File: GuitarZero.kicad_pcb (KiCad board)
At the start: 6 copper layers, 144 parts, among them J1 USB_A, J2 USB_B_Micro, J3 AudioJack3_SwitchT, J4 MCU_Debug, J6 Micro_SD_Card_Det_Hirose_DM3AT, SW1 SW_Push, SW2 SW_Push, SW3 SW_Push, SW4 SW_Push, SW5 SW_Push, SW6 SW_Push, U1 TPS54325, U10 FPGA_GPIO_Extra, U11 5x7 LED_matrix, U12 MCU_GPIO_Extra, U13 5x7 LED_matrix, U14 Power_Jumpers, U2 TSP54294, U3 XC7A100T-FTG256, U4 EFM32GG332, U5 S25FL127S, U6 Oscillator, U7 FPGA_JTAG_Debug, U8 PCM1754, U9 TPD_Current_Switch, Y1 Crystal_GND23

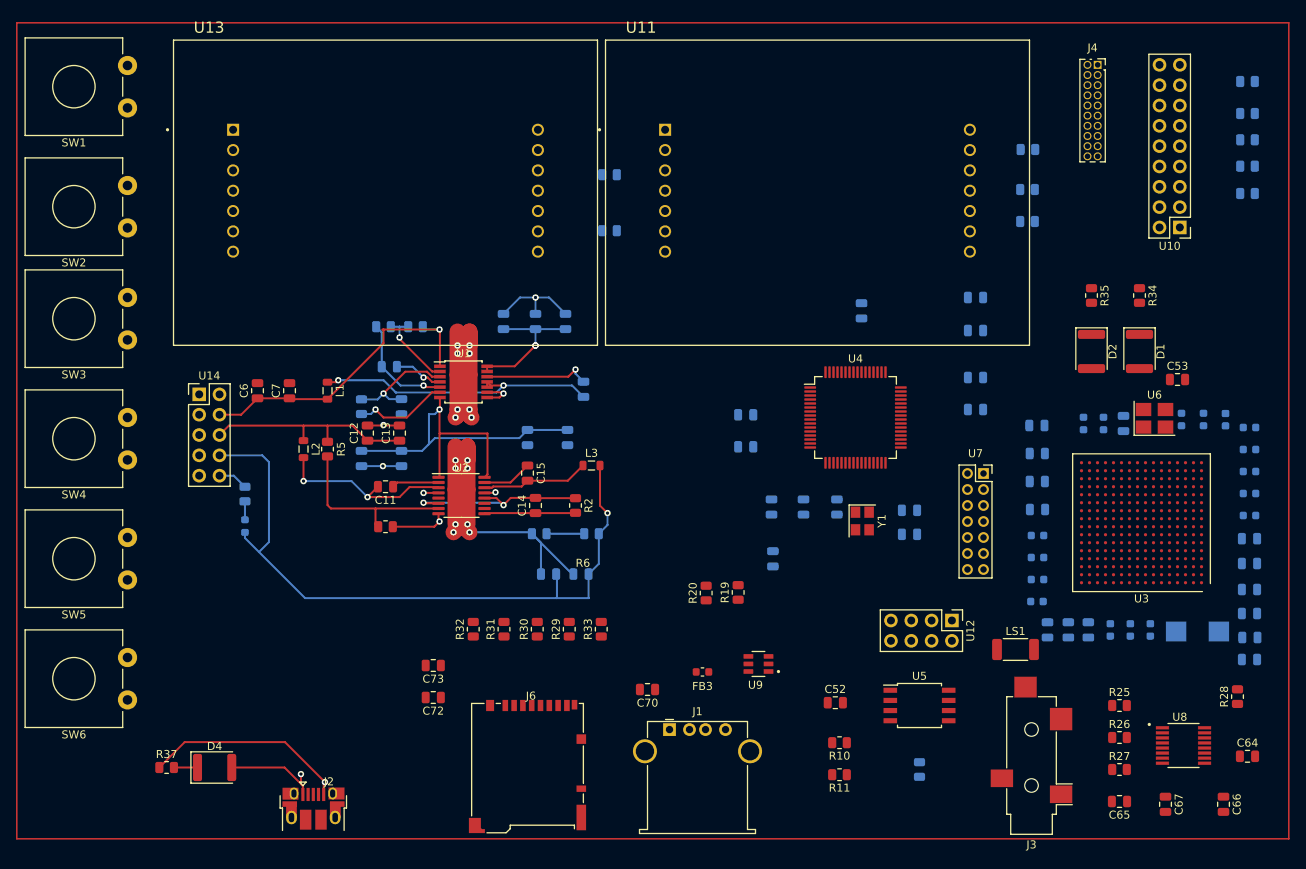
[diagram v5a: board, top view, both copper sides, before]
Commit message: Wired MCU in .pcb
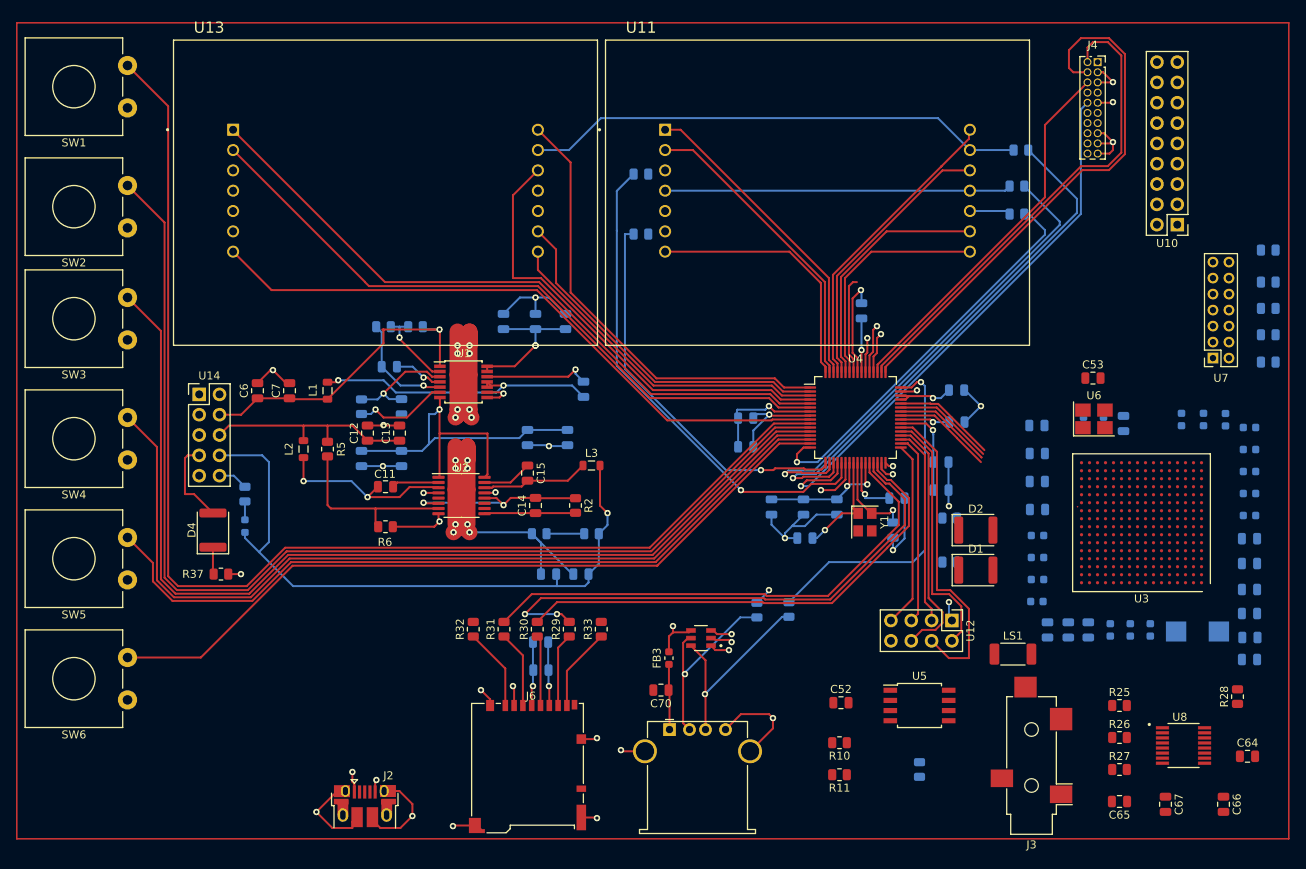
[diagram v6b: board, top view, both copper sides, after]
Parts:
- C72, C73, R19, R20, R34, R35: moved to B.Cu
- moved R34 40.9 mm to (173.8, 108.1), turned to 180 degrees
- moved D1 34.1 mm to (177.0, 109.1), turned to 0 degrees
- moved R35 33.0 mm to (173.8, 102.6), turned to 180 degrees
- moved U7 32.1 mm to (206.7, 82.6), turned to 180 degrees
- moved D4 29.7 mm to (81.7, 104.1), turned to 90 degrees
- moved D2 26.6 mm to (177.0, 104.1), turned to 0 degrees
- moved R37 25.1 mm to (82.7, 109.6), turned to 180 degrees
- moved R13 21.2 mm to (213.6, 69.1)
- moved R14 21.2 mm to (213.6, 73.1)
- moved R16 21.2 mm to (213.6, 79.7)
- moved R17 21.2 mm to (213.6, 83.1)
- moved R15 21.2 mm to (213.6, 76.4)
- moved C55 21.0 mm to (172.7, 95.6)
- moved C54 20.4 mm to (172.7, 99.1)
- moved C59 17.3 mm to (167.2, 100.1), turned to 0 degrees
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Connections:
- D4 pad 2: +5V -> +3.3V
- R18 pad 1: Net-(U11-R5) -> Net-(U11-R2)
- R21 pad 1: Net-(U11-R4) -> Net-(U11-R1)
- R23 pad 1: Net-(U11-R2) -> Net-(U11-R5)
- R24 pad 1: Net-(U11-R1) -> Net-(U11-R4)
- U11 pad 12: Net-(U4-PE12) -> Net-(U4-PE11)
- U11 pad 5: Net-(U4-PE12) -> unconnected-(U11-C4-Pad5)
- U13 pad 12: Net-(U4-PC3) -> Net-(U4-PA3)
- U13 pad 4: Net-(R22-Pad1) -> unconnected-(U13-R3-Pad4)
- U13 pad 5: Net-(U4-PC3) -> unconnected-(U13-C4-Pad5)
- U4 pad 1: /MCU/Button 1 -> Net-(U13-C6)
- U4 pad 10: Net-(U13-C2) -> /MCU/Button 1
- U4 pad 11: Net-(U13-C3) -> /MCU/Button 2
- U4 pad 12: Net-(U4-PC3) -> /MCU/Button 3
- U4 pad 13: Net-(U13-C5) -> /MCU/Button 4
- U4 pad 14: Net-(U13-C6) -> /MCU/Button 5
- U4 pad 15: Net-(U13-C7) -> /MCU/Button 6
- U4 pad 2: /MCU/Button 2 -> Net-(U13-C7)
- U4 pad 3: /MCU/Button 3 -> Net-(U13-C5)
- U4 pad 37: Net-(U12-GPIO_4) -> Net-(U12-GPIO_2)
- U4 pad 38: Net-(U12-GPIO_2) -> Net-(U12-GPIO_4)
- U4 pad 4: /MCU/Button 4 -> Net-(U4-PA3)
- U4 pad 5: /MCU/Button 5 -> Net-(U13-C3)
- U4 pad 58: Net-(U11-C1) -> Net-(U11-C5)
- U4 pad 59: Net-(U11-C2) -> Net-(U11-C7)
- U4 pad 6: /MCU/Button 6 -> Net-(U13-C1)
- U4 pad 60: Net-(U11-C3) -> Net-(U4-PE11)
- U4 pad 61: Net-(U4-PE12) -> Net-(U11-C6)
- U4 pad 62: Net-(U11-C5) -> Net-(U11-C3)
- U4 pad 63: Net-(U11-C6) -> Net-(U11-C1)
- U4 pad 64: Net-(U11-C7) -> Net-(U11-C2)
- U4 pad 9: Net-(U13-C1) -> Net-(U13-C2)
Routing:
- net /MCU/Button 1: track 0.00 -> 155.1 mm
- net /MCU/Button 2: track 0.00 -> 140.7 mm
- net GND: track 143.0 -> 270.6 mm, vias 25 -> 49
- net /MCU/Button 3: track 0.00 -> 127.2 mm
- net /MCU/Button 4: track 0.00 -> 112.8 mm
- net /MCU/Button 5: track 0.00 -> 98.3 mm
- net /MCU/Button 6: track 0.00 -> 96.4 mm
- net Net-(U13-C3): track 0.00 -> 86.3 mm
- net Net-(U13-C1): track 0.00 -> 85.5 mm
- net Net-(U13-C2): track 0.00 -> 80.9 mm
- net Net-(J4-RESET): track 0.00 -> 69.9 mm, vias 0 -> 1
- net +3.3V: track 0.00 -> 68.0 mm, vias 0 -> 6
- net Net-(U4-PD1): track 0.00 -> 67.9 mm, vias 0 -> 2
- net Net-(J4-SWCLK): track 0.00 -> 67.3 mm
- net Net-(J6-DAT3/CD): track 0.00 -> 66.2 mm, vias 0 -> 2
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
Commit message: completed DAC
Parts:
- moved C66 8.37 mm to (199.7, 137.6)
- moved C67 3.01 mm to (203.7, 137.6)
- moved R27 1.22 mm to (194.2, 133.1)
- moved C65 0.70 mm to (195.7, 138.0)
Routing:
- net GND: track 270.6 -> 319.7 mm, vias 49 -> 53
- net /DAC/OUT_RIGHT: track 0.00 -> 25.6 mm
- net /DAC/OUT_LEFT: track 0.00 -> 19.9 mm
- net +5V: track 201.7 -> 210.3 mm
- net Net-(U8-VoutL): track 0.00 -> 7.02 mm
- net Net-(U8-LRCK): track 0.00 -> 6.47 mm
- net Net-(U8-BCK): track 0.00 -> 5.61 mm
- net Net-(U8-SCK): track 0.00 -> 5.35 mm
- net Net-(U8-VoutR): track 0.00 -> 4.77 mm
- net Net-(U8-DATA): track 0.00 -> 4.70 mm
- net Net-(U8-Vcom): track 0.00 -> 4.52 mm
- net Net-(J3-PadTN): track 0.00 -> 4.43 mm

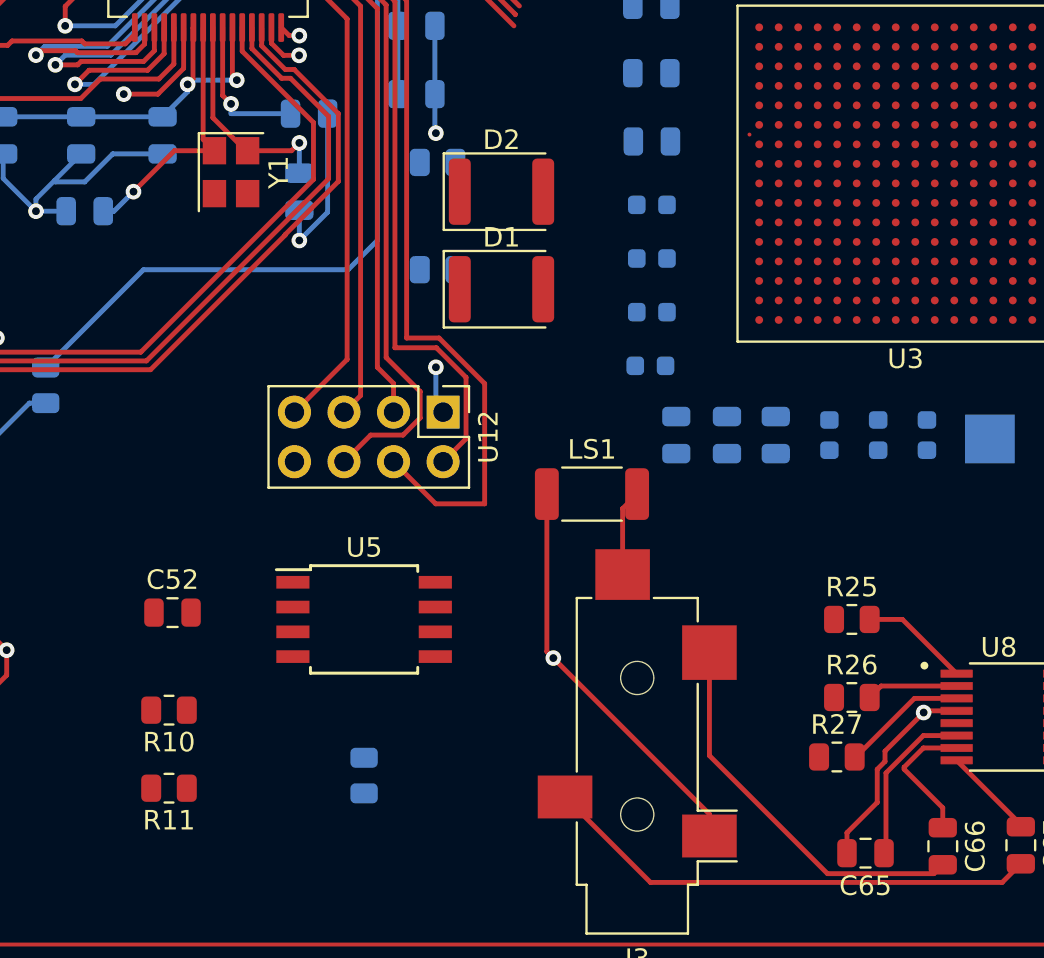
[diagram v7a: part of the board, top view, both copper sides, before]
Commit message: FPGA - SPI Flash Memory
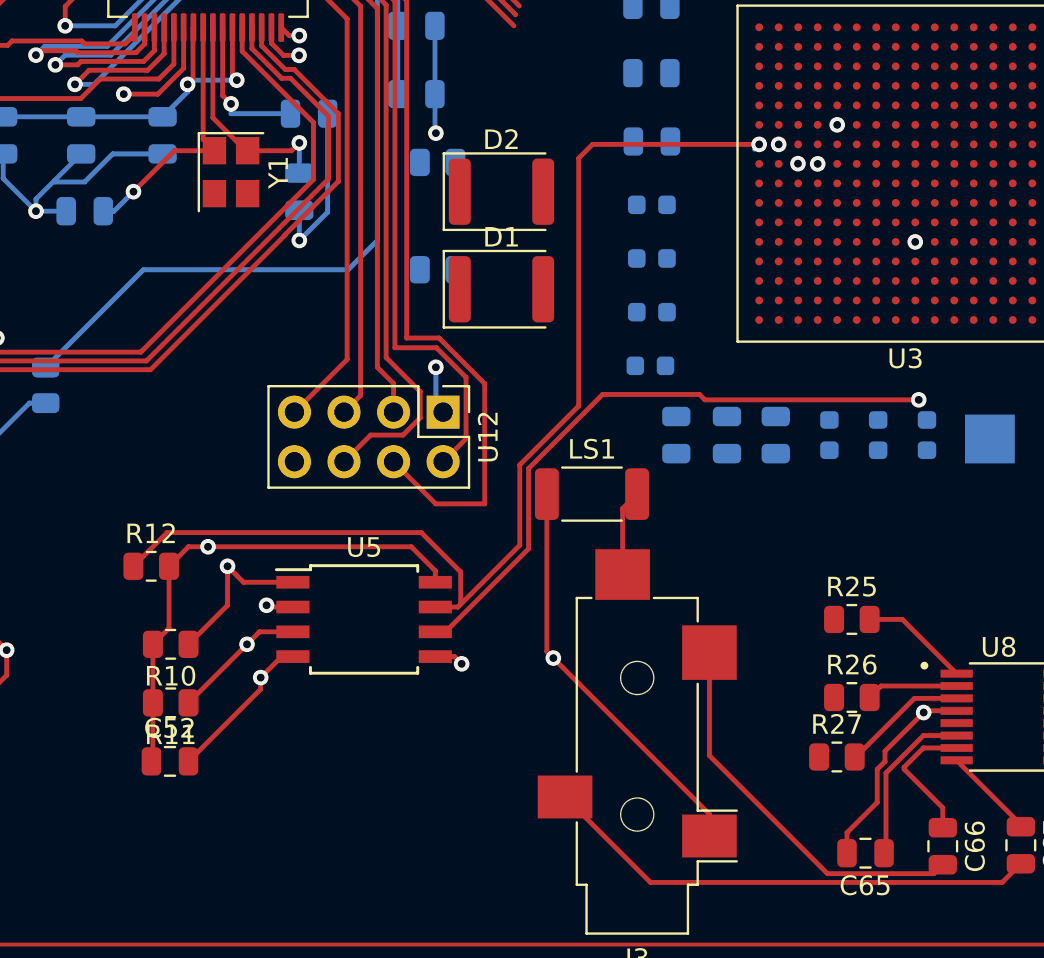
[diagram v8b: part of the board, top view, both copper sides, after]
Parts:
- R12: moved to F.Cu
- moved R12 15.3 mm to (159.1, 123.3), turned to 0 degrees
- moved C52 7.63 mm to (160.1, 133.3)
- moved R11 4.38 mm to (160.1, 130.3)
- moved R10 3.38 mm to (160.1, 127.3)
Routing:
- net Net-(U3A-IO_L6P_T0_FCS_B_14): track 0.00 -> 57.8 mm, vias 0 -> 2
- net Net-(U3A-IO_L2N_T0_D03_14): track 0.00 -> 56.6 mm, vias 0 -> 1
- net Net-(U3A-IO_L2P_T0_D02_14): track 0.00 -> 53.4 mm, vias 0 -> 2
- net Net-(U3A-IO_L1P_T0_D00_MOSI_14): track 0.00 -> 49.5 mm, vias 0 -> 2
- net Net-(U3A-IO_L1N_T0_D01_DIN_14): track 0.00 -> 45.8 mm, vias 0 -> 2
- net Net-(U3C-CCLK_0): track 0.00 -> 41.4 mm, vias 0 -> 2
- net +3.3V: track 68.0 -> 93.5 mm, vias 6 -> 7
- net GND: track 319.7 -> 327.6 mm, vias 53 -> 54
